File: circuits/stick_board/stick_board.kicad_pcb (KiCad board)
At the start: 2 copper layers, 113.2 x 22.8 mm, 0 parts

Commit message: layout  摇杆板轮廓
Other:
- board size 113.2 x 22.8 mm -> 129.2 x 51.2 mm
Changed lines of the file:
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@@
   )
   (net 0 "")
+  (gr_line (start 205.7 134.875) (end 205.7 131.55)
+    (stroke (width 0.1) (type default)) (layer "Edge.Cuts"))
+  (gr_line (start 82.475 136.525) (end 76.5 134.875)
+    (stroke (width 0.1) (type default)) (layer "Edge.Cuts"))
+  (gr_circle (center 195.325 133.6) (end 196.625 133.6)
+    (stroke (width 0.1) (type default)) (fill none) (layer "Edge.Cuts"))
+  (gr_line (start 179.3 147.2) (end 179.3 142)
+    (stroke (width 0.1) (type default)) (layer "Edge.Cuts"))
+  (gr_line (start 205.7 131.55) (end 203.625 127)
+    (stroke (width 0.1) (type default)) (layer "Edge.Cuts"))
+  (gr_line (start 82.475 136.525) (end 83.35 135.8)
+    (stroke (width 0.1) (type default)) (layer "Edge.Cuts"))
   (gr_line (start 111.7 122.3) (end 111.7 100.5)
+    (stroke (width 0.1) (type default)) (layer "Edge.Cuts"))
+  (gr_line (start 76.5 131.55) (end 78.575 127)
+    (stroke (width 0.1) (type default)) (layer "Edge.Cuts"))
+  (gr_line (start 104.4 149.1) (end 102.9 147.2)
     (stroke (width 0.1) (type default)) (layer "Edge.Cuts"))
   (gr_circle (center 86 101) (end 87.5 101)
     (stroke (width 0.1) (type default)) (fill none) (layer "Edge.Cuts"))
+  (gr_line (start 199.725 136.525) (end 205.7 134.875)
+    (stroke (width 0.1) (type default)) (layer "Edge.Cuts"))
+  (gr_line (start 177.8 149.1) (end 179.3 147.2)
+    (stroke (width 0.1) (type default)) (layer "Edge.Cuts"))
+  (gr_line (start 90.775 137.725) (end 83.35 135.8)
+    (stroke (width 0.1) (type default)) (layer "Edge.Cuts"))
+  (gr_line (start 78.575 127) (end 78.1 125.25)
+    (stroke (width 0.1) (type default)) (layer "Edge.Cuts"))
   (gr_line (start 111.7 122.3) (end 170.5 122.3)
+    (stroke (width 0.1) (type default)) (layer "Edge.Cuts"))
+  (gr_line (start 90.975 138.925) (end 90.775 137.725)
+    (stroke (width 0.1) (type default)) (layer "Edge.Cuts"))
+  (gr_circle (center 86.875 133.6) (end 88.175 133.5)
+    (stroke (width 0.1) (type default)) (fill none) (layer "Edge.Cuts"))
+  (gr_line (start 76.5 134.875) (end 76.5 131.55)
+    (stroke (width 0.1) (type default)) (layer "Edge.Cuts"))
+  (gr_line (start 194.9 97.9) (end 197.64 97.9)
+    (stroke (width 0.1) (type default)) (layer "Edge.Cuts"))
+  (gr_line (start 102.9 147.2) (end 102.9 142)
+    (stroke (width 0.1) (type default)) (layer "Edge.Cuts"))
+  (gr_line (start 193 100.50868) (end 194.9 97.9)
+    (stroke (width 0.1) (type default)) (layer "Edge.Cuts"))
+  (gr_line (start 83.314672 99.555654) (end 83.329344 102.89132)
+    (stroke (width 0.1) (type default)) (layer "Edge.Cuts"))
+  (gr_line (start 191.225 138.925) (end 191.425 137.725)
+    (stroke (width 0.1) (type default)) (layer "Edge.Cuts"))
+  (gr_line (start 203.625 127) (end 204.1 125.25)
+    (stroke (width 0.1) (type default)) (layer "Edge.Cuts"))
+  (gr_line (start 199 102.9) (end 204.1 125.25)
+    (stroke (width 0.1) (type default)) (layer "Edge.Cuts"))
+  (gr_line (start 170.5 100.5) (end 193 100.50868)
+    (stroke (width 0.1) (type default)) (layer "Edge.Cuts"))
+  (gr_line (start 191.425 137.725) (end 198.85 135.8)
+    (stroke (width 0.1) (type default)) (layer "Edge.Cuts"))
+  (gr_line (start 83.314672 99.555654) (end 84.9 97.89132)
+    (stroke (width 0.1) (type default)) (layer "Edge.Cuts"))
+  (gr_line (start 78.1 125.25) (end 83.329344 102.89132)
+    (stroke (width 0.1) (type default)) (layer "Edge.Cuts"))
+  (gr_line (start 111.7 100.5) (end 89.3 100.5)
+    (stroke (width 0.1) (type default)) (layer "Edge.Cuts"))
+  (gr_line (start 87.4 97.89132) (end 89.3 100.5)
     (stroke (width 0.1) (type default)) (layer "Edge.Cuts"))
   (gr_line (start 170.5 122.3) (end 170.5 100.5)
     (stroke (width 0.1) (type default)) (layer "Edge.Cuts"))
+  (gr_line (start 87.4 97.89132) (end 84.9 97.89132)
+    (stroke (width 0.1) (type default)) (layer "Edge.Cuts"))
+  (gr_circle (center 78.75 132.8) (end 80 132.8)
+    (stroke (width 0.1) (type default)) (fill none) (layer "Edge.Cuts"))
+  (gr_line (start 104.4 149.1) (end 177.8 149.1)
+    (stroke (width 0.1) (type default)) (layer "Edge.Cuts"))
   (gr_circle (center 196.2 101) (end 197.7 101)
     (stroke (width 0.1) (type default)) (fill none) (layer "Edge.Cuts"))
+  (gr_circle (center 203.45 132.8) (end 204.7 132.8)
+    (stroke (width 0.1) (type default)) (fill none) (layer "Edge.Cuts"))
+  (gr_line (start 179.3 142) (end 191.225 138.925)
+    (stroke (width 0.1) (type default)) (layer "Edge.Cuts"))
+  (gr_line (start 198.85 135.8) (end 199.725 136.525)
+    (stroke (width 0.1) (type default)) (layer "Edge.Cuts"))
+  (gr_line (start 199 102.9) (end 198.985328 99.564334)
+    (stroke (width 0.1) (type default)) (layer "Edge.Cuts"))
+  (gr_line (start 102.9 142) (end 90.975 138.925)
+    (stroke (width 0.1) (type default)) (layer "Edge.Cuts"))
+  (gr_line (start 197.64 97.9) (end 198.985328 99.564334)
+    (stroke (width 0.1) (type default)) (layer "Edge.Cuts"))
 )

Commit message: layout 摇杆板布局ok
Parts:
- added BTN_B1: SW_PUSH, stick:touch, F.Cu at (191.2, 108.0)
- added C1: 100nF, Resistor_SMD:R_0805_2012Metric_Pad1.20x1.40mm_HandSolder, B.Cu at (101.6, 108.9)
- added C2: 100nF, Resistor_SMD:R_0805_2012Metric_Pad1.20x1.40mm_HandSolder, B.Cu at (187.2, 104.4)
- added C3: 100nF, Resistor_SMD:R_0805_2012Metric_Pad1.20x1.40mm_HandSolder, F.Cu at (104.2, 123.8)
- added C4: 100nF, Resistor_SMD:R_0805_2012Metric_Pad1.20x1.40mm_HandSolder, F.Cu at (162.2, 144.2)
- added D1: D, Diode_SMD:D_0805_2012Metric_Pad1.15x1.40mm_HandSolder, F.Cu at (92.4, 122.4)
- added D2: D, Diode_SMD:D_0805_2012Metric_Pad1.15x1.40mm_HandSolder, F.Cu at (193.5, 124.3)
- added J1: Conn_01x13_Pin, Connector_FFC-FPC:Molex_200528-0130_1x13-1MP_P1.00mm_Horizontal, F.Cu at (131.8, 142.5)
- added M1: Motor_DC, Resistor_SMD:R_1210_3225Metric_Pad1.30x2.65mm_HandSolder, F.Cu at (84.5, 125.2)
- added M2: Motor_DC, Resistor_SMD:R_1210_3225Metric_Pad1.30x2.65mm_HandSolder, F.Cu at (197.8, 125.6)
- added Q1: AO3400A, Package_TO_SOT_SMD:SOT-23-3, F.Cu at (93.7, 126.5)
- added Q2: AO3400A, Package_TO_SOT_SMD:SOT-23-3, F.Cu at (188.0, 124.3)
- added R1: 1M, Resistor_SMD:R_0805_2012Metric_Pad1.20x1.40mm_HandSolder, F.Cu at (100.8, 122.9)
- added R13: 10K, Resistor_SMD:R_0805_2012Metric_Pad1.20x1.40mm_HandSolder, F.Cu at (97.9, 128.2)
- added R14: 10K, Resistor_SMD:R_0805_2012Metric_Pad1.20x1.40mm_HandSolder, F.Cu at (185.3, 119.4)
- added R2: 1M, Resistor_SMD:R_0805_2012Metric_Pad1.20x1.40mm_HandSolder, F.Cu at (157.8, 144.2)
- added R20: 10R, Resistor_SMD:R_1206_3216Metric_Pad1.30x1.75mm_HandSolder, F.Cu at (97.9, 122.7)
- added R21: 10R, Resistor_SMD:R_1206_3216Metric_Pad1.30x1.75mm_HandSolder, F.Cu at (182.3, 122.9)
- added U1: GULI, stick:GULI, F.Cu at (101.7, 108.6)
- added U2: GULI, stick:GULI, F.Cu at (161.1, 131.9)
- added U3: DRV5055A1xDBZxQ1, Package_TO_SOT_SMD:SOT-23-3, B.Cu at (101.3, 104.3)
- added U4: DRV5055A1xDBZxQ1, Package_TO_SOT_SMD:SOT-23-3, B.Cu at (180.9, 104.3)

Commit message: layout  摇杆板完成
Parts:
- C4, M1, M2, R2: moved to B.Cu
- moved R1 3.65 mm to (104.4, 122.3)
- moved C3 2.92 mm to (101.7, 122.3), turned to -90 degrees
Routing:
- net +3V3: track 0.00 -> 281.9 mm, vias 0 -> 8
- net GND: track 0.00 -> 215.1 mm, vias 0 -> 7
- net /RIGHT_HALL: track 0.00 -> 85.5 mm, vias 0 -> 1
- net /BTN_B: track 0.00 -> 84.8 mm
- net /MOTOR2: track 0.00 -> 73.0 mm, vias 0 -> 4
- net /LEFT_BTN: track 0.00 -> 68.2 mm, vias 0 -> 1
- net /LEFT_HALL: track 0.00 -> 57.2 mm, vias 0 -> 3
- net /MOTOR1: track 0.00 -> 48.7 mm
- net /RIGHT_X: track 0.00 -> 46.3 mm, vias 0 -> 2
- net /LEFT_Y: track 0.00 -> 45.3 mm, vias 0 -> 1
- net /LEFT_X: track 0.00 -> 43.8 mm, vias 0 -> 2
- net Net-(U2-Shield): track 0.00 -> 42.3 mm
- net /RIGHT_BTN: track 0.00 -> 41.1 mm, vias 0 -> 1
- net Net-(U1-Shield): track 0.00 -> 40.7 mm
- net /RIGHT_Y: track 0.00 -> 39.7 mm, vias 0 -> 1
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- added copper zone on B.Cu, net GND
- added copper zone on F.Cu, net GND

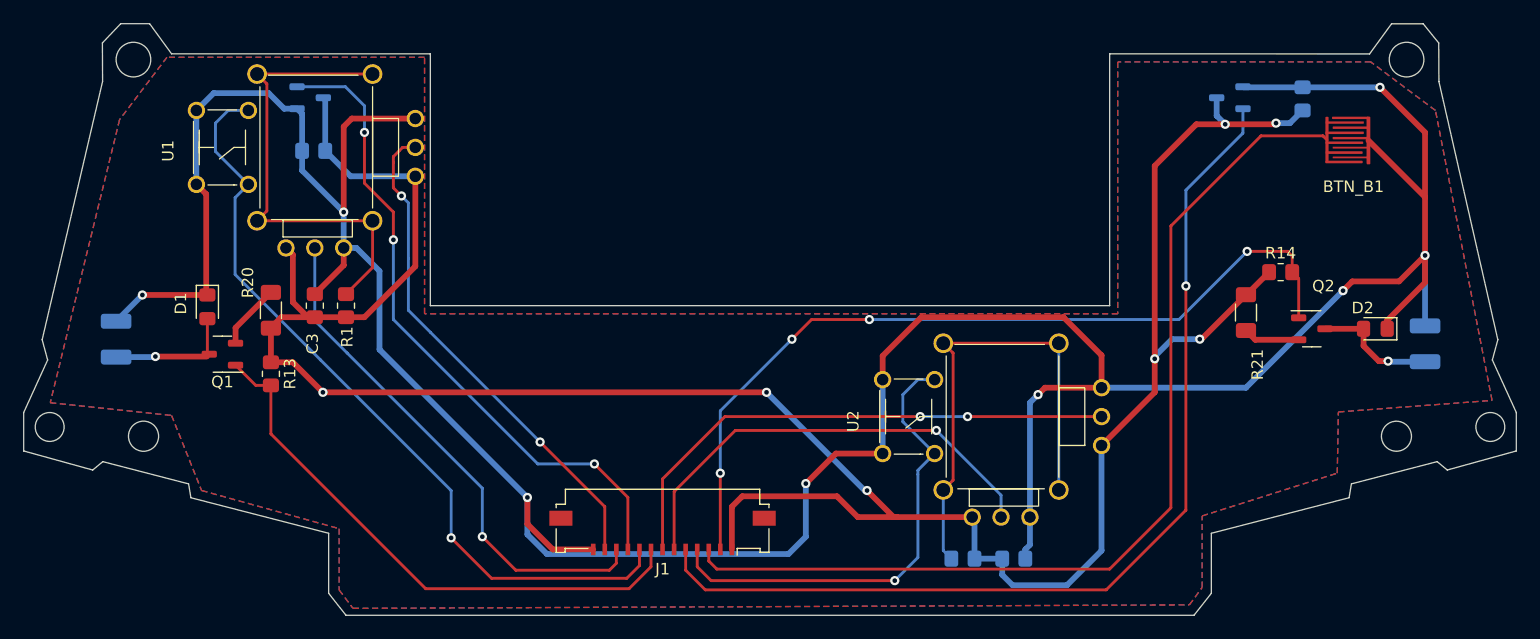
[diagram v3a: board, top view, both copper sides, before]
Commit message: layout  摇杆板优化马达驱动,增加覆铜过孔         MCU板改动
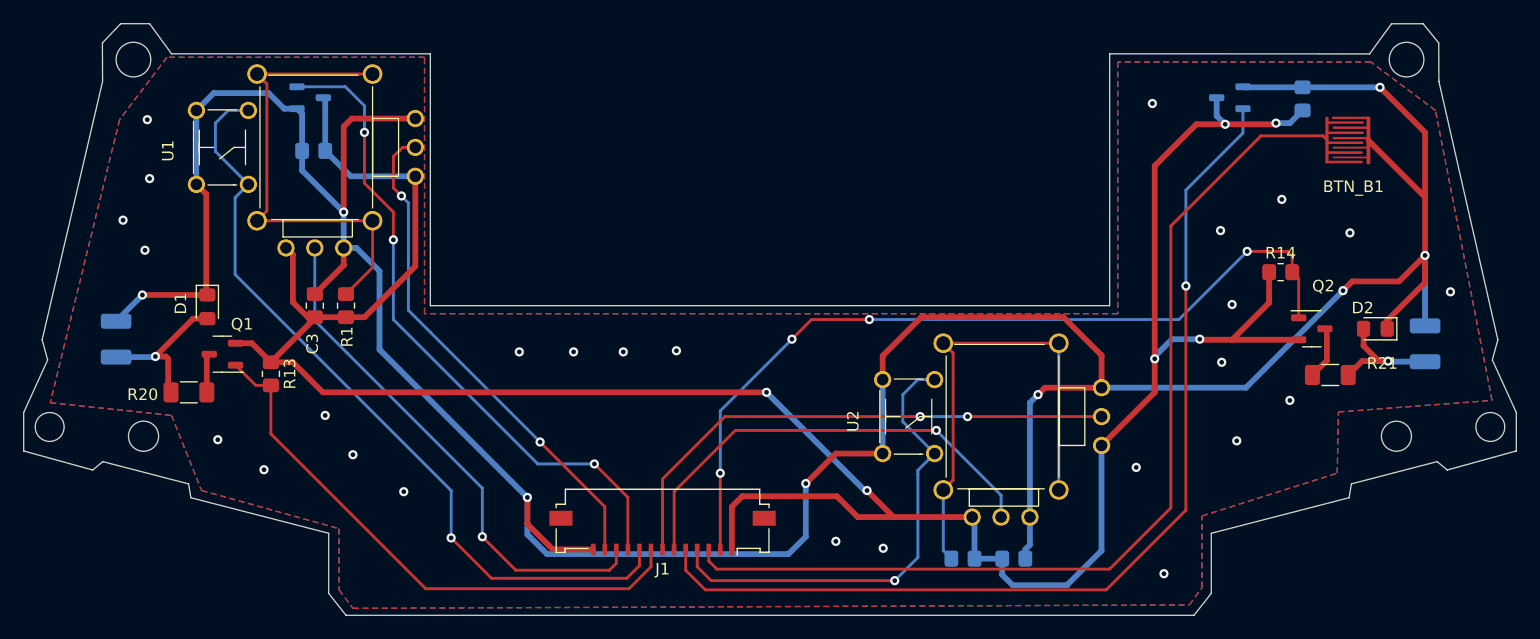
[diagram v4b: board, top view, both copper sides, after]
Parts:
- moved R20 10.0 mm to (90.8, 129.8), turned to 180 degrees
- moved R21 9.08 mm to (189.6, 128.3), turned to 0 degrees
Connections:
- Q1 pad 2: Net-(Q1-S) -> GND
- Q1 pad 3: Net-(D1-A) -> Net-(Q1-D)
- Q2 pad 2: Net-(Q2-S) -> GND
- Q2 pad 3: Net-(D2-A) -> Net-(Q2-D)
- R20 pad 1: GND -> Net-(Q1-D)
- R20 pad 2: Net-(Q1-S) -> Net-(D1-A)
- R21 pad 1: GND -> Net-(Q2-D)
- R21 pad 2: Net-(Q2-S) -> Net-(D2-A)
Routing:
- net GND: track 215.1 -> 224.6 mm, vias 7 -> 32
- net Net-(Q1-S): track 5.67 -> 0.00 mm
- net Net-(Q2-S): track 4.89 -> 0.00 mm
- net Net-(Q2-D): track 0.00 -> 4.59 mm
- net Net-(Q1-D): track 0.00 -> 3.62 mm
- net Net-(D1-A): track 11.0 -> 13.5 mm
